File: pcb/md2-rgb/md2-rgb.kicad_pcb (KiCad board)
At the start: 2 copper layers, 55.8 x 32.8 mm, 23 parts, among them J101 MD-90SM, J102 MD-90SM

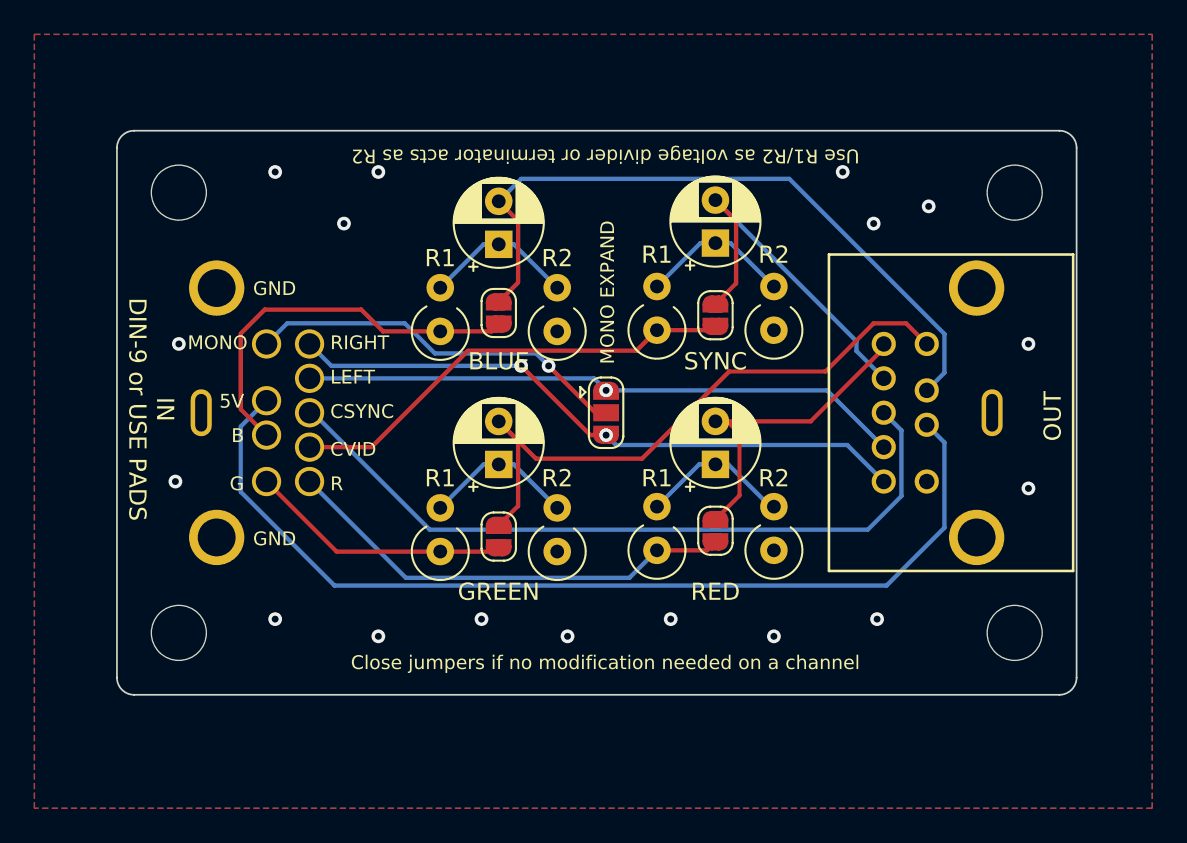
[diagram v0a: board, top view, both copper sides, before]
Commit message: Adds FPC to RGB breakout
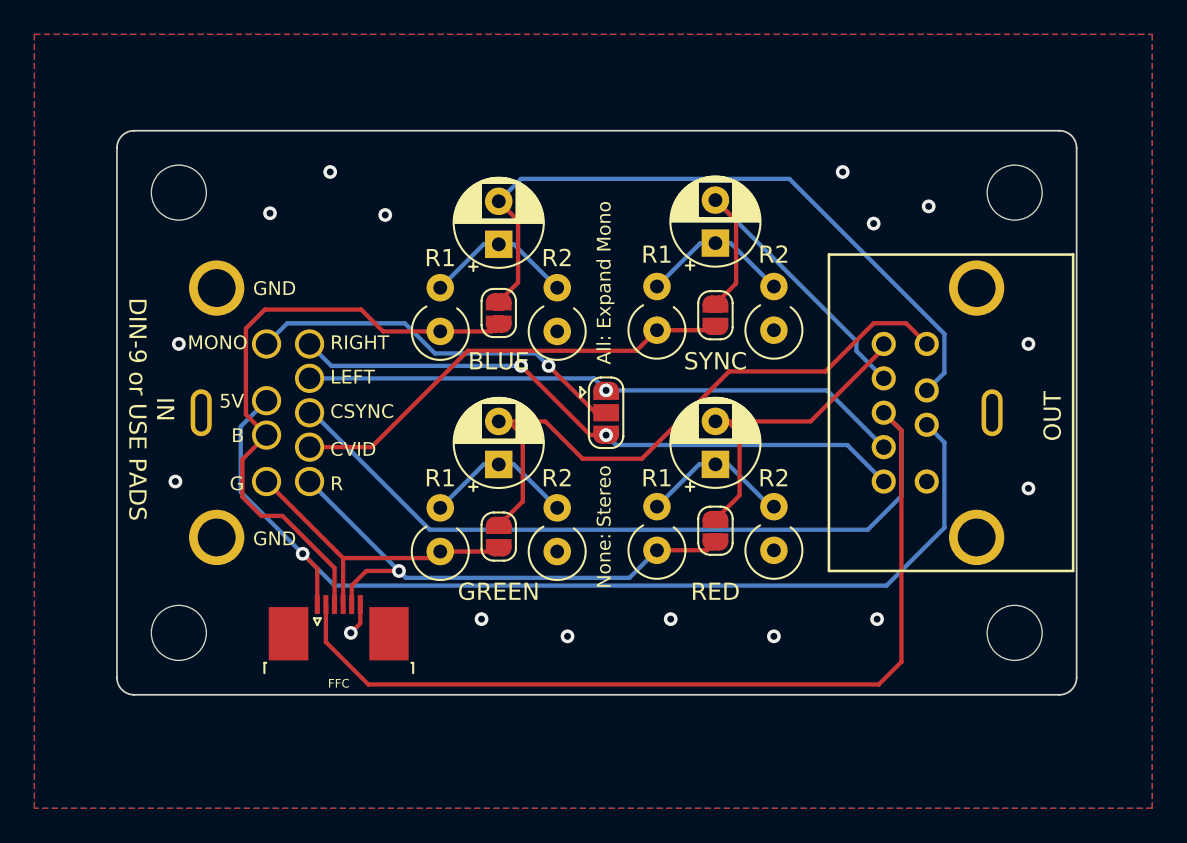
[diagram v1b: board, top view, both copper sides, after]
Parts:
- added J1: FFC, Connector_FFC-FPC:TE_0-1734839-6_1x06-1MP_P0.5mm_Horizontal, F.Cu at (97.7, 114.5)
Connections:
- net Net-(J101-5V) renamed /VCC
- net Net-(J101-CSYNC) renamed /CVID
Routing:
- net /CVID: track 43.3 -> 95.4 mm
- net /B_IN: track 22.8 -> 35.9 mm
- net /R_IN: track 26.8 -> 31.0 mm, vias 0 -> 1
- net /VCC: track 56.9 -> 60.2 mm, vias 0 -> 1
- net /G_IN: track 15.3 -> 18.3 mm
- net GND: track 0.00 -> 1.88 mm, vias 17 -> 16
- net /G_OUT: track 36.5 -> 37.1 mm
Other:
- board text added: "All: Expand Mono"
- board text added: "Close jumpers if no modification needed on a channel Otherwise R1 and C are required"
- board text added: "None: Stereo"
- board text added: "Use R1/R2 as voltage divider or assume 75R terminator acts as R2"
- board text removed: "Close jumpers if no modification needed on a channel"
- board text removed: "MONO EXPAND"
- board text removed: "Use R1/R2 as voltage divider or terminator acts as R2"

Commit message: Flips FFC
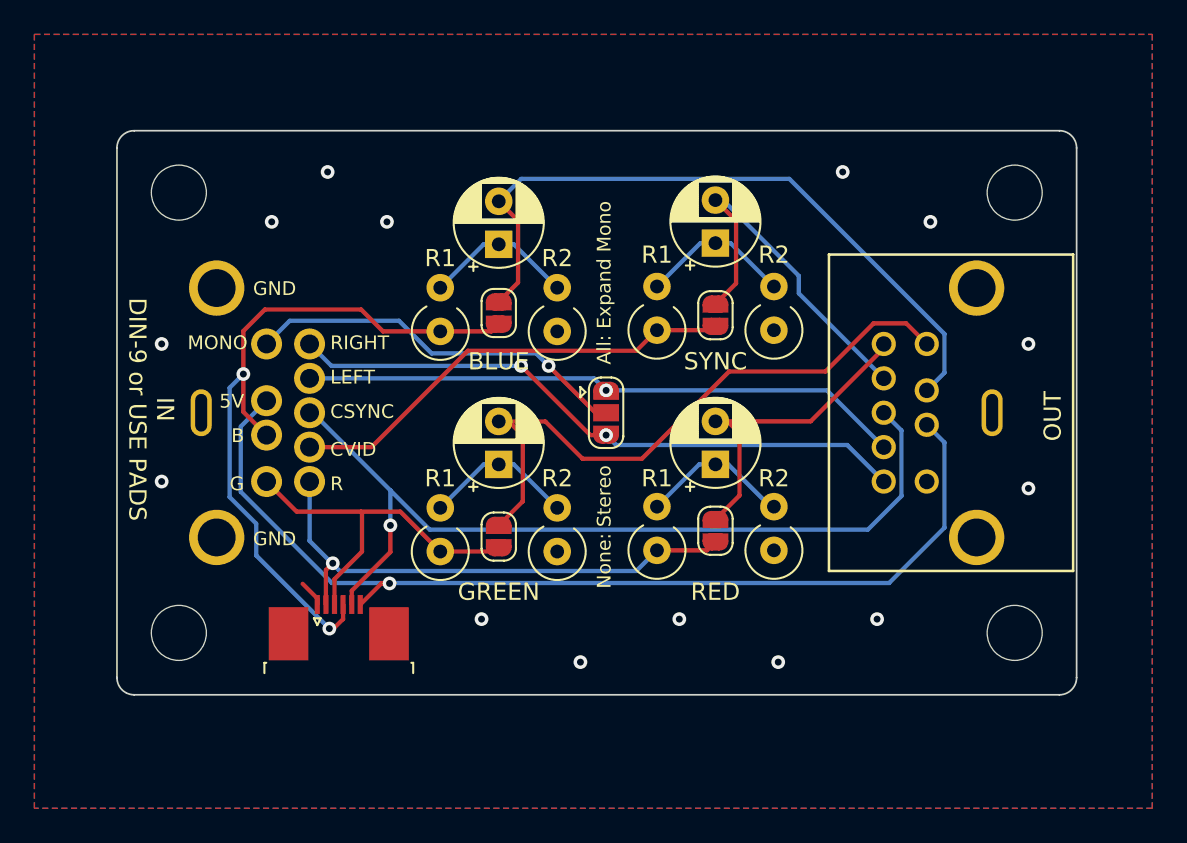
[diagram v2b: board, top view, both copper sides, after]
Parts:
- J1: value FFC -> Conn_01x06_Pin
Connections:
- J1 pad 1: /VCC -> GND
- J1 pad 2: /CVID -> /R_IN
- J1 pad 3: /B_IN -> /G_IN
- J1 pad 4: /G_IN -> /B_IN
- J1 pad 5: /R_IN -> /CVID
- J1 pad 6: GND -> /VCC
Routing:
- net /CVID: track 95.4 -> 50.9 mm, vias 0 -> 1
- net /B_IN: track 35.9 -> 42.1 mm, vias 0 -> 2
- net /G_IN: track 18.3 -> 21.4 mm
- net /VCC: track 60.2 -> 59.0 mm
- net GND: track 1.88 -> 1.55 mm, vias 16 -> 14

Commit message: connects FFC to composite in, not sync
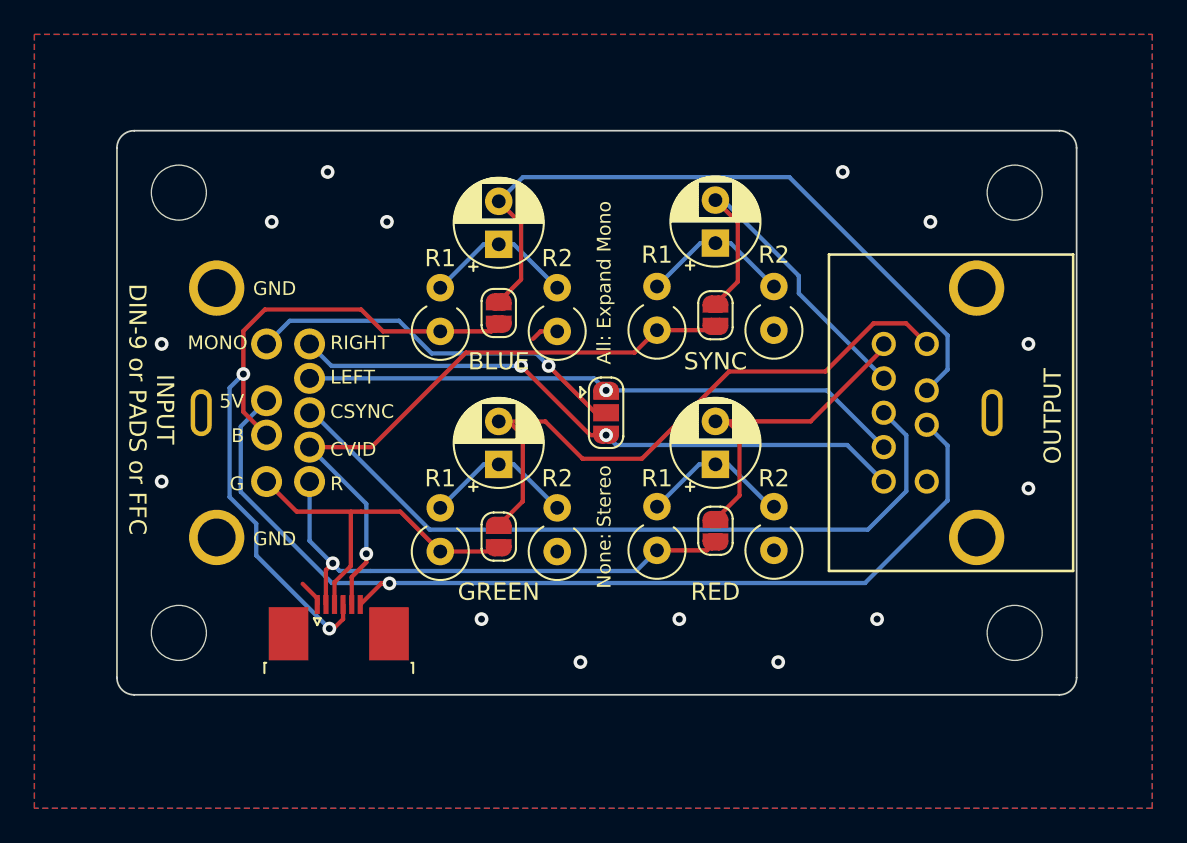
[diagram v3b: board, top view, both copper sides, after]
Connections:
- J1 pad 5: /CVID -> /C_IN
- J101 pad 5: /CVID -> /CSYNC
- J102 pad 5: /CVID -> /CSYNC
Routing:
- net /CVID: track 50.9 -> 0.00 mm, vias 1 -> 0
- net /CSYNC: track 0.00 -> 43.5 mm
- net /C_IN: track 26.5 -> 37.4 mm, vias 0 -> 1
- net GND: track 1.55 -> 3.13 mm
- net /VCC: track 59.0 -> 58.3 mm
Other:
- board text added: "INPUT DIN-9 or PADS or FFC"
- board text added: "JLCJLCJLCJLCJLC"
- board text added: "OUTPUT"
- board text removed: "IN DIN-9 or USE PADS"
- board text removed: "OUT"
